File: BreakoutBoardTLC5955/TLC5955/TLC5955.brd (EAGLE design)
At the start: 45.7 x 71.1 mm, 3 parts

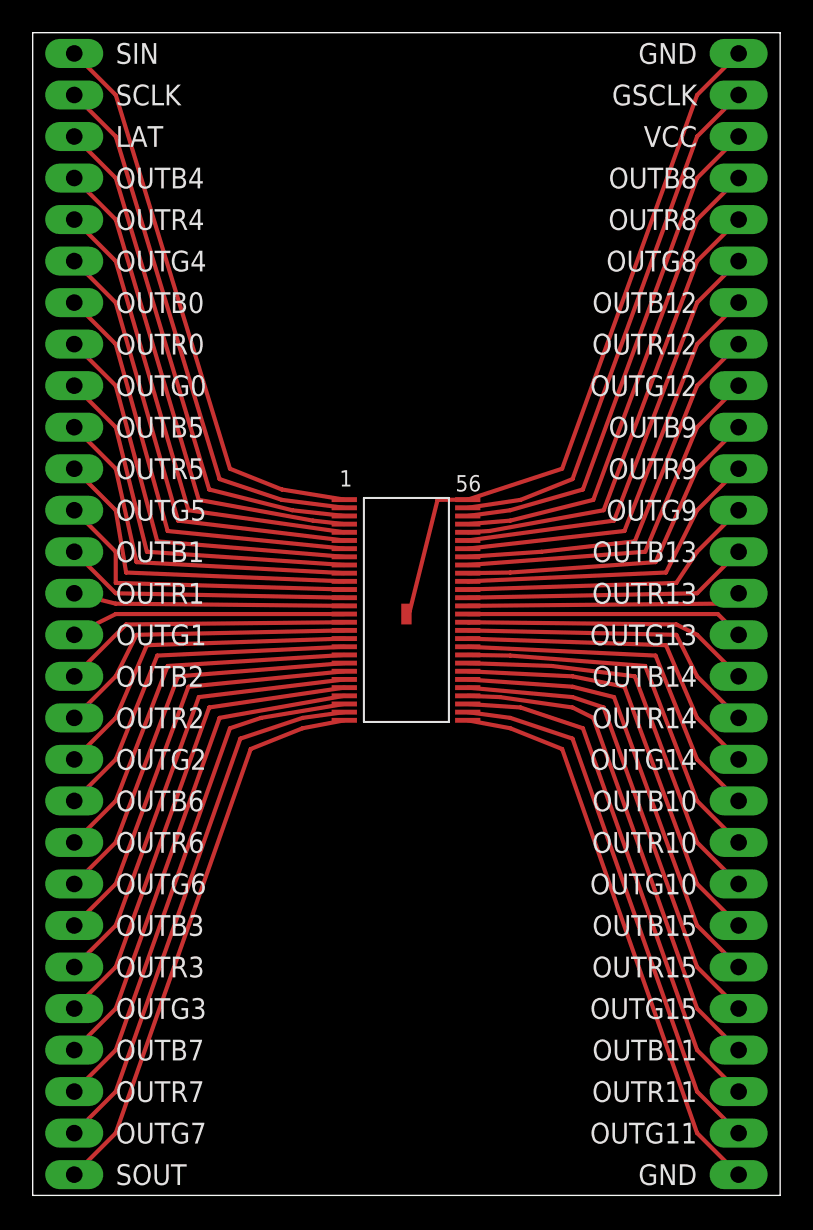
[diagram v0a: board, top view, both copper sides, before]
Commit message: Updated TLC5955 Breakout
Made 1” in size
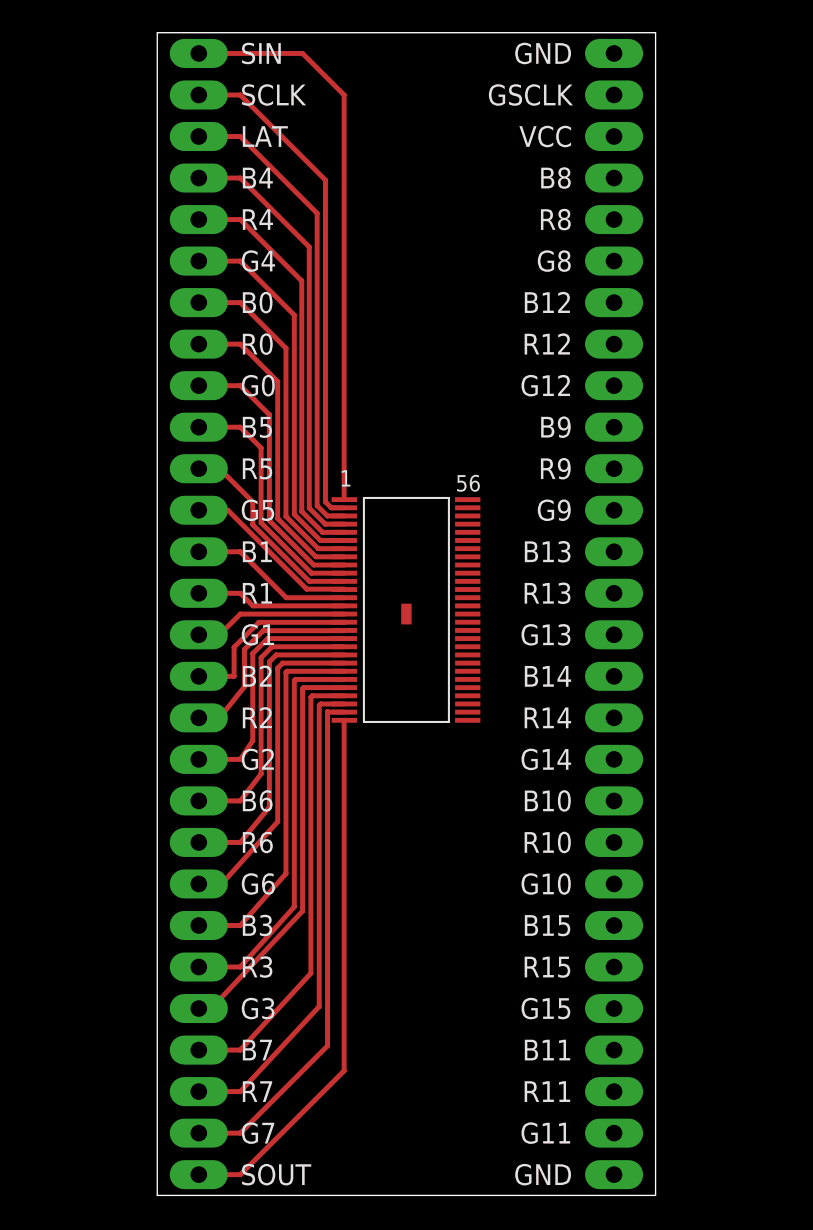
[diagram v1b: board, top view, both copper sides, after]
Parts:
- moved U$2 7.62 mm to (10.2, 35.6)
- moved U$3 7.62 mm to (35.6, 35.6)
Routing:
- net N$29: track 43.1 -> 0.00 mm
- net N$32: track 34.6 -> 0.00 mm
- net N$33: track 33.1 -> 0.00 mm
- net N$56: track 32.6 -> 0.00 mm
- net N$34: track 31.7 -> 0.00 mm
- net N$31: track 31.1 -> 0.00 mm
- net N$35: track 30.3 -> 0.00 mm
- net N$55: track 29.7 -> 0.00 mm
- net N$36: track 28.9 -> 0.00 mm
- net N$54: track 28.3 -> 0.00 mm
- net N$37: track 27.5 -> 0.00 mm
- net N$53: track 26.9 -> 0.00 mm
- net N$38: track 26.1 -> 0.00 mm
- net N$52: track 25.5 -> 0.00 mm
- net N$39: track 24.7 -> 0.00 mm
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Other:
- board size 45.7 x 71.1 mm -> 30.5 x 71.1 mm
- board text added: "B0"
- board text added: "B1"
- board text added: "B10"
- board text added: "B11"
- board text added: "B12"
- board text added: "B13"
- board text added: "B14"
- board text added: "B15"
- board text added: "B2"
- board text added: "B3"
- board text added: "B4"
- board text added: "B5"
- board text added: "B6"
- board text added: "B7"
- board text added: "B8"
- board text added: "B9"
- board text added: "G0"
- board text added: "G1"
- board text added: "G10"
- board text added: "G11"
- board text added: "G12"
- board text added: "G13"
- board text added: "G14"
- board text added: "G15"
- board text added: "G2"
- board text added: "G3"
- board text added: "G4"
- board text added: "G5"
- board text added: "G6"
- board text added: "G7"
- board text added: "G8"
- board text added: "G9"
- board text added: "R0"
- board text added: "R1"
- board text added: "R10"
- board text added: "R11"
- board text added: "R12"
- board text added: "R13"
- board text added: "R14"
- board text added: "R15"
- board text added: "R2"
- board text added: "R3"
- board text added: "R4"
- board text added: "R5"
- board text added: "R6"
- board text added: "R7"
- board text added: "R8"
- board text added: "R9"
- board text removed: "OUTB0"
- board text removed: "OUTB1"
- board text removed: "OUTB10"
- board text removed: "OUTB11"
- board text removed: "OUTB12"
- board text removed: "OUTB13"
- board text removed: "OUTB14"
- board text removed: "OUTB15"
- board text removed: "OUTB2"
- board text removed: "OUTB3"
- board text removed: "OUTB4"
- board text removed: "OUTB5"
- board text removed: "OUTB6"
- board text removed: "OUTB7"
- board text removed: "OUTB8"
- board text removed: "OUTB9"
- board text removed: "OUTG0"
- board text removed: "OUTG1"
- board text removed: "OUTG10"
- board text removed: "OUTG11"
- board text removed: "OUTG12"
- board text removed: "OUTG13"
- board text removed: "OUTG14"
- board text removed: "OUTG15"
- board text removed: "OUTG2"
- board text removed: "OUTG3"
- board text removed: "OUTG4"
- board text removed: "OUTG5"
- board text removed: "OUTG6"
- board text removed: "OUTG7"
- board text removed: "OUTG8"
- board text removed: "OUTG9"
- board text removed: "OUTR0"
- board text removed: "OUTR1"
- board text removed: "OUTR10"
- board text removed: "OUTR11"
- board text removed: "OUTR12"
- board text removed: "OUTR13"
- board text removed: "OUTR14"
- board text removed: "OUTR15"
- board text removed: "OUTR2"
- board text removed: "OUTR3"
- board text removed: "OUTR4"
- board text removed: "OUTR5"
- board text removed: "OUTR6"
- board text removed: "OUTR7"
- board text removed: "OUTR8"
- board text removed: "OUTR9"

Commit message: TLC Breakout added cap, having trouble with crossed airwires
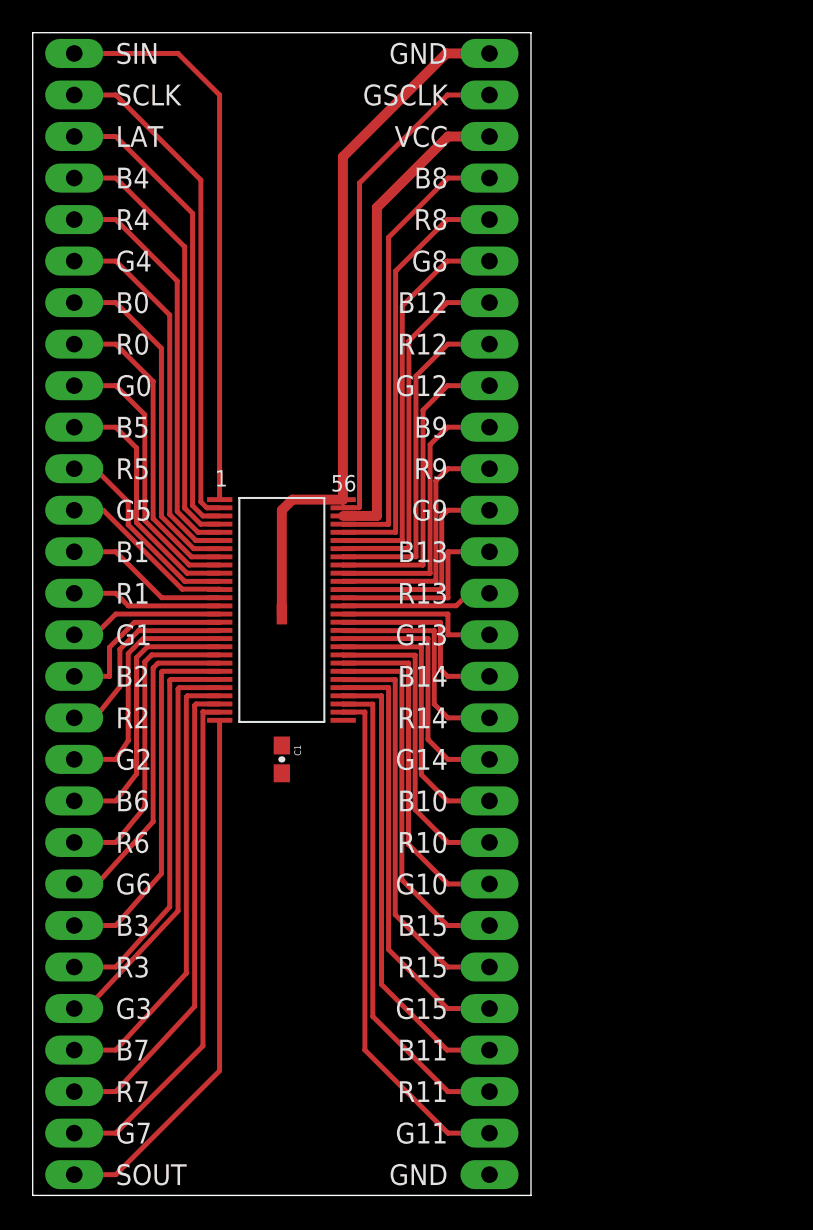
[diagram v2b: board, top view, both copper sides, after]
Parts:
- added C1: 0.1uF, SparkFun-Capacitors:0603-CAP
- moved U$3 7.62 mm to (27.9, 35.6)
- moved U$2 7.62 mm to (2.54, 35.6)
- moved U$1 7.62 mm to (15.2, 35.6)
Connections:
- removed net N$29: U$1.P$1, U$1.P56, U$3.P28
- removed net N$32: U$1.P29, U$3.P1
- new net N$57: C1.2, U$1.P$1, U$1.P29, U$1.P56, U$3.P1, U$3.P28
- net N$31: now also C1.1
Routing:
- net N$57: track 0.00 -> 42.9 mm
- net N$33: track 0.00 -> 31.7 mm
- net N$56: track 0.00 -> 31.0 mm
- net N$34: track 0.00 -> 30.0 mm
- net N$31: track 0.00 -> 29.6 mm
- net N$35: track 0.00 -> 28.3 mm
- net N$55: track 0.00 -> 28.0 mm
- net N$36: track 0.00 -> 26.5 mm
- net N$54: track 0.00 -> 26.2 mm
- net N$37: track 0.00 -> 24.7 mm
- net N$53: track 0.00 -> 24.4 mm
- net N$38: track 0.00 -> 22.9 mm
- net N$52: track 0.00 -> 22.6 mm
- net N$39: track 0.00 -> 21.1 mm
- net N$51: track 0.00 -> 20.8 mm
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
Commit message: Updated TLC board, added .lck files to gitignore
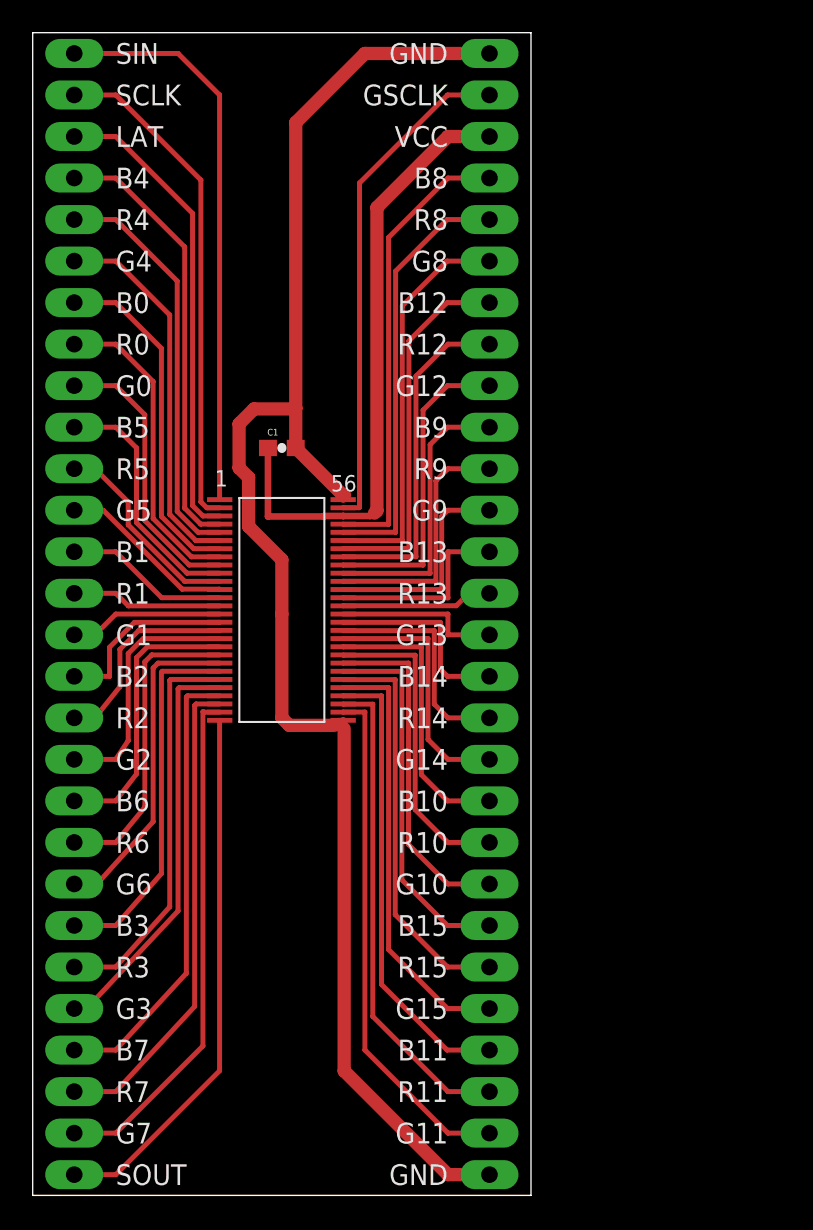
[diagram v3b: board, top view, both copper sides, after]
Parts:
- C1: value 0.1uF -> 10uF; device SparkFun-Capacitors:0603-CAP -> WallerLabLib:0603-CAP
- moved C1 19.0 mm to (15.2, 45.7), turned to 0 degrees
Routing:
- net N$57: track 42.9 -> 98.0 mm
- net N$31: track 29.6 -> 38.3 mm
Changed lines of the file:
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@@
 <?xml version="1.0" encoding="utf-8"?>
 <!DOCTYPE eagle SYSTEM "eagle.dtd">
-<eagle version="7.4.0">
+<eagle version="7.5.0">
 <drawing>
 <settings>
@@
 <setting verticaltext="up"/>
 </settings>
-<grid distance="0.05" unitdist="inch" unit="inch" style="lines" multiple="1" display="yes" altdistance="0.001" altunitdist="inch" altunit="inch"/>
+<grid distance="0.05" unitdist="inch" unit="inch" style="lines" multiple="1" display="yes" altdistance="0.005" altunitdist="inch" altunit="inch"/>
 <layers>
 <layer number="1" name="Top" color="4" fill="1" visible="yes" active="yes"/>
@@
 <element name="U$2" library="WallerLabLib" package="28PIN_HOLES" value="28_PINS0" x="2.54" y="35.56" rot="R270"/>
 <element name="U$3" library="WallerLabLib" package="28PIN_HOLES" value="28_PINS0" x="27.94" y="35.56" rot="R90"/>
-<element name="C1" library="SparkFun-Capacitors" package="0603-CAP" value="0.1uF" x="15.24" y="26.67" rot="R270">
-<attribute name="PROD_ID" value="CAP-00810" x="15.24" y="26.67" size="1.778" layer="27" rot="R270" display="off"/>
+<element name="C1" library="WallerLabLib" package="0603-CAP" value="10uF" x="15.24" y="45.72">
+<attribute name="PROD_ID" value="CAP-11015" x="15.24" y="45.72" size="1.778" layer="27" display="off"/>
 </element>
 </elements>
@@
 <wire x1="2.54" y1="69.85" x2="8.89" y2="69.85" width="0.3048" layer="1"/>
 <wire x1="8.89" y1="69.85" x2="11.43" y2="67.31" width="0.3048" layer="1"/>
+<wire x1="11.43" y1="42.57" x2="11.44" y2="42.56" width="0.3048" layer="1"/>
 <wire x1="11.43" y1="67.31" x2="11.43" y2="42.57" width="0.3048" layer="1"/>
-<wire x1="11.43" y1="42.57" x2="11.44" y2="42.56" width="0.3048" layer="1"/>
 </signal>
 <signal name="N$27">
@@
 <contactref element="U$1" pad="P54"/>
 <contactref element="U$3" pad="P26"/>
-<wire x1="18.99" y1="41.56" x2="21.0566" y2="41.56" width="0.6096" layer="1"/>
-<wire x1="21.0566" y1="41.56" x2="21.0566" y2="60.4266" width="0.6096" layer="1"/>
-<wire x1="21.0566" y1="60.4266" x2="25.4" y2="64.77" width="0.6096" layer="1"/>
-<wire x1="25.4" y1="64.77" x2="27.94" y2="64.77" width="0.6096" layer="1"/>
 <contactref element="C1" pad="1"/>
-<wire x1="15.24" y1="27.52" x2="18.99" y2="41.56" width="0" layer="19" extent="1-1"/>
+<wire x1="18.99" y1="41.56" x2="17.8054" y2="41.56" width="0.4064" layer="1"/>
+<wire x1="17.8054" y1="41.56" x2="17.8054" y2="41.529" width="0.4064" layer="1"/>
+<wire x1="17.8054" y1="41.529" x2="14.39" y2="41.529" width="0.4064" layer="1"/>
+<wire x1="14.39" y1="41.529" x2="14.39" y2="45.72" width="0.4064" layer="1"/>
+<wire x1="21.0566" y1="41.8846" x2="21.0566" y2="60.4266" width="0.8128" layer="1"/>
+<wire x1="21.0566" y1="60.4266" x2="25.4" y2="64.77" width="0.8128" layer="1"/>
+<wire x1="25.4" y1="64.77" x2="27.94" y2="64.77" width="0.8128" layer="1"/>
+<wire x1="21.0566" y1="41.8846" x2="20.9042" y2="41.7322" width="0.8128" layer="1"/>
+<wire x1="20.9042" y1="41.7322" x2="20.828" y2="41.7322" width="0.4064" layer="1"/>
+<wire x1="20.828" y1="41.7322" x2="20.6502" y2="41.5544" width="0.4064" layer="1"/>
+<wire x1="20.6502" y1="41.5544" x2="18.9956" y2="41.5544" width="0.4064" layer="1"/>
+<wire x1="18.9956" y1="41.5544" x2="18.99" y2="41.56" width="0.4064" layer="1"/>
 </signal>
 <signal name="N$33">
@@
 <contactref element="U$1" pad="P56"/>
 <contactref element="U$1" pad="P29"/>
-<wire x1="18.99" y1="29.06" x2="15.24" y2="35.56" width="0" layer="19" extent="1-1"/>
-<wire x1="15.24" y1="25.82" x2="18.99" y2="29.06" width="0" layer="19" extent="1-1"/>
-<wire x1="27.94" y1="1.27" x2="15.24" y2="25.82" width="0" layer="19" extent="1-1"/>
-<wire x1="27.94" y1="69.85" x2="25.2984" y2="69.85" width="0.6096" layer="1"/>
-<wire x1="25.2984" y1="69.85" x2="18.9738" y2="63.5254" width="0.6096" layer="1"/>
-<wire x1="18.9738" y1="63.5254" x2="18.9738" y2="42.5762" width="0.6096" layer="1"/>
-<wire x1="18.9738" y1="42.5762" x2="18.99" y2="42.56" width="0.6096" layer="1"/>
-<wire x1="18.99" y1="42.56" x2="15.89" y2="42.56" width="0.6096" layer="1"/>
-<wire x1="15.89" y1="42.56" x2="15.24" y2="41.91" width="0.6096" layer="1"/>
-<wire x1="15.24" y1="41.91" x2="15.24" y2="35.56" width="0.6096" layer="1"/>
+<wire x1="18.99" y1="29.0068" x2="18.99" y2="29.06" width="0.4064" layer="1"/>
+<wire x1="18.99" y1="29.0068" x2="19.05" y2="29.0068" width="0.4064" layer="1"/>
+<wire x1="19.05" y1="29.0068" x2="19.05" y2="28.5496" width="0.4064" layer="1"/>
+<wire x1="19.05" y1="28.5496" x2="19.05" y2="7.62" width="0.8128" layer="1"/>
+<wire x1="19.05" y1="7.62" x2="25.4" y2="1.27" width="0.8128" layer="1"/>
+<wire x1="25.4" y1="1.27" x2="27.94" y2="1.27" width="0.8128" layer="1"/>
+<wire x1="18.99" y1="29.0068" x2="18.6944" y2="29.0068" width="0.4064" layer="1"/>
+<wire x1="18.6944" y1="29.0068" x2="18.4404" y2="28.7528" width="0.4064" layer="1"/>
+<wire x1="18.4404" y1="28.7528" x2="15.6972" y2="28.7528" width="0.8128" layer="1"/>
+<wire x1="15.6972" y1="28.7528" x2="15.24" y2="29.21" width="0.8128" layer="1"/>
+<wire x1="15.24" y1="29.21" x2="15.24" y2="35.56" width="0.8128" layer="1"/>
+<wire x1="18.99" y1="42.56" x2="18.99" y2="42.7644" width="0.4064" layer="1"/>
+<wire x1="18.99" y1="42.7644" x2="19.0754" y2="42.8498" width="0.4064" layer="1"/>
+<wire x1="19.0754" y1="42.8498" x2="18.9602" y2="42.8498" width="0.8128" layer="1"/>
+<wire x1="18.9602" y1="42.8498" x2="16.09" y2="45.72" width="0.8128" layer="1"/>
+<wire x1="16.09" y1="45.72" x2="16.09" y2="48.1584" width="0.8128" layer="1"/>
+<wire x1="16.09" y1="48.1584" x2="16.09" y2="65.62" width="0.8128" layer="1"/>
+<wire x1="16.09" y1="65.62" x2="20.32" y2="69.85" width="0.8128" layer="1"/>
+<wire x1="20.32" y1="69.85" x2="27.94" y2="69.85" width="0.8128" layer="1"/>
+<wire x1="15.24" y1="35.56" x2="15.24" y2="38.8874" width="0.8128" layer="1"/>
+<wire x1="15.24" y1="38.8874" x2="13.208" y2="40.9194" width="0.8128" layer="1"/>
+<wire x1="13.208" y1="40.9194" x2="13.208" y2="43.9166" width="0.8128" layer="1"/>
+<wire x1="13.208" y1="43.9166" x2="12.6238" y2="44.5008" width="0.8128" layer="1"/>
+<wire x1="12.6238" y1="44.5008" x2="12.6238" y2="47.1932" width="0.8128" layer="1"/>
+<wire x1="12.6238" y1="47.1932" x2="13.5382" y2="48.1076" width="0.8128" layer="1"/>
+<wire x1="13.5382" y1="48.1076" x2="16.0392" y2="48.1076" width="0.8128" layer="1"/>
+<wire x1="16.0392" y1="48.1076" x2="16.09" y2="48.1584" width="0.8128" layer="1"/>
 </signal>
 </signals>

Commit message: Fixed TLC5955 right side
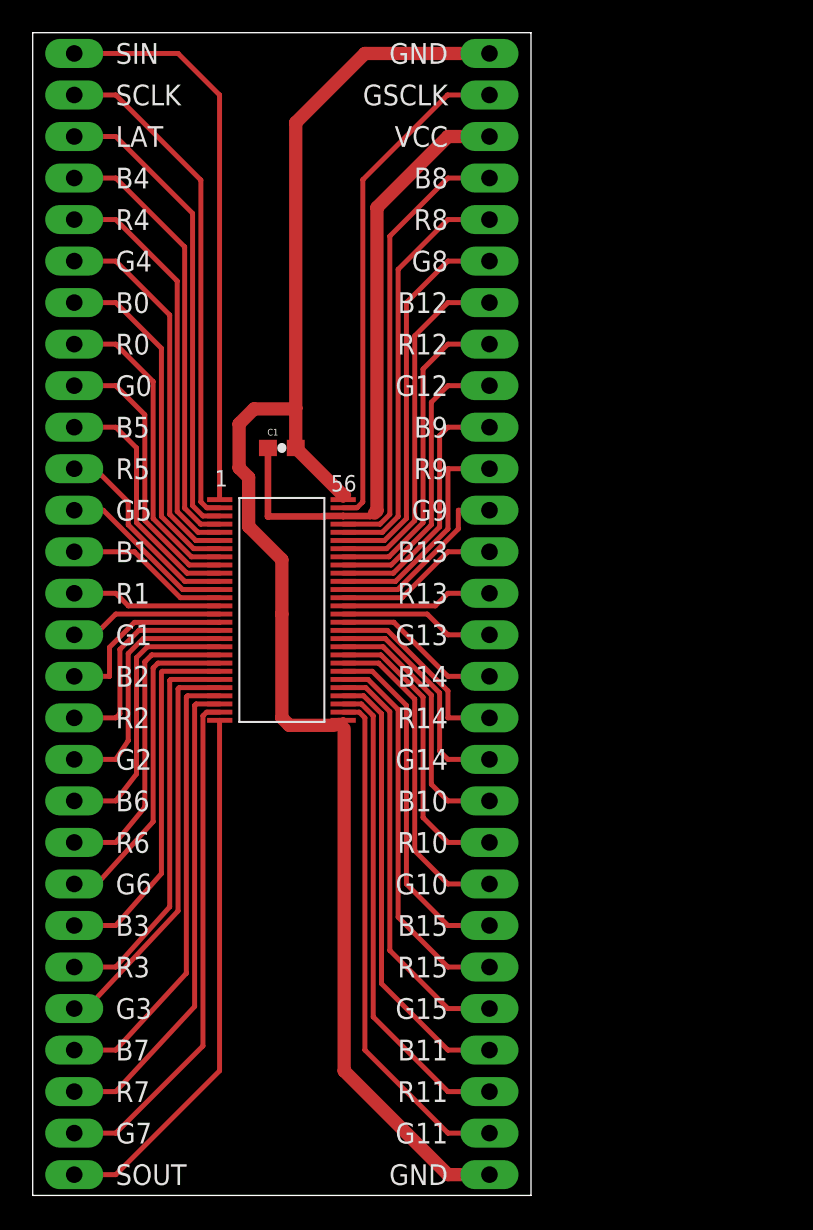
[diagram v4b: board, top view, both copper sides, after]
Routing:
- net N$48: track 13.6 -> 11.6 mm
- net N$44: track 12.0 -> 10.3 mm
- net N$43: track 13.8 -> 12.1 mm
- net N$47: track 11.8 -> 10.1 mm
- net N$42: track 15.6 -> 14.1 mm
- net N$49: track 15.4 -> 14.0 mm
- net N$41: track 17.4 -> 16.1 mm
- net N$30: track 17.3 -> 15.9 mm
- net N$40: track 19.2 -> 18.0 mm
- net N$50: track 19.0 -> 17.9 mm
- net N$39: track 21.1 -> 20.0 mm
- net N$38: track 22.9 -> 21.8 mm
- net N$37: track 24.7 -> 23.7 mm
- net N$51: track 20.8 -> 19.8 mm
- net N$14: track 12.6 -> 13.4 mm
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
